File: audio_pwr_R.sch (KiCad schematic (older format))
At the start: 40 parts, among them Q201 BC546, Q202 BC546, Q203 BC546, Q204 BD140, Q205 BC546, Q206 BD139, Q207 BD140, Q208 MJL21193, Q209 MJL21194

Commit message: Opened on home office computer. Some rescue and lib conversion happened. Need to confirm no changes on work laptop.
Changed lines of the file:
@@
 EESchema Schematic File Version 4
-LIBS:AAMB-cache
 EELAYER 30 0
 EELAYER END
@@
 	2600 3650 2450 3650
 $Comp
-L Power-amp:+35V #PWR0110
+L AAMB-rescue:+35V-Power-amp #PWR0110
 U 1 1 5E2254A5
 P 8025 1725
@@
 	8025 1900 8025 1725
 $Comp
-L Power-amp:-35V #PWR0111
+L AAMB-rescue:-35V-Power-amp #PWR0111
 U 1 1 5E229770
 P 8025 5100

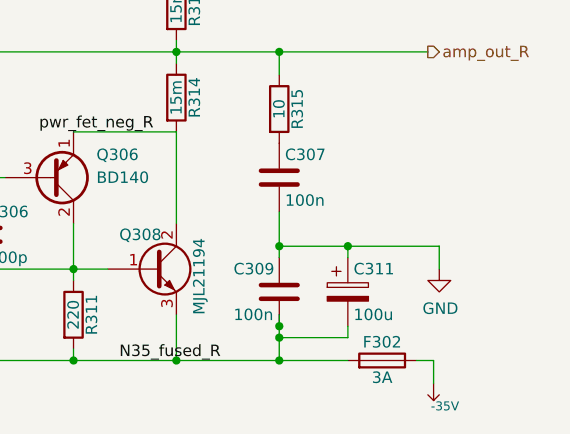
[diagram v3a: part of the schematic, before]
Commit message: Fixed several DRC errors. Tied audoi input returns to GND. Added Switch logic.
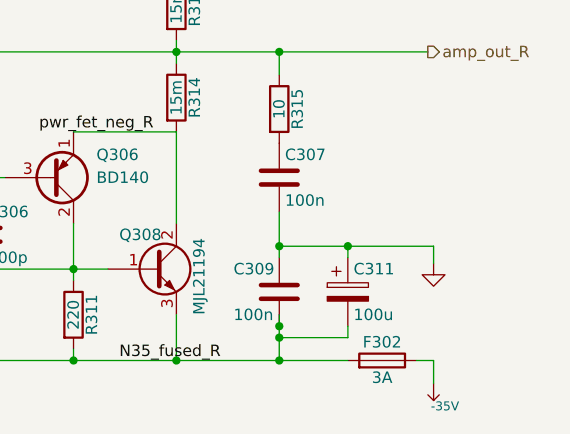
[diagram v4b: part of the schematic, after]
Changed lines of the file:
@@
 EESchema Schematic File Version 4
+LIBS:AAMB-cache
 EELAYER 30 0
 EELAYER END
@@
 Wire Wire Line
 	7300 2050 7300 2100
-Connection ~ 7650 4500
 Connection ~ 3300 3800
 Wire Wire Line
@@
 Wire Wire Line
 	7450 2450 7450 2500
-$Comp
-L power:GND #PWR04
-U 1 1 5C7F686C
-P 8050 4600
-AR Path="/5C7F608F/5C7F686C" Ref="#PWR04"  Part="1"
-AR Path="/5C814038/5C7F686C" Ref="#PWR0304"  Part="1"
-AR Path="/5E252703/5C7F686C" Ref="#PWR?"  Part="1"
-F 0 "#PWR0304" H 8050 4350 50  0001 C CNN
-F 1 "GND" H 8055 4427 50  0000 C CNN
-F 2 "" H 8050 4600 50  0001 C CNN
-F 3 "" H 8050 4600 50  0001 C CNN
-	1    8050 4600
-	1    0    0    -1
-$EndComp
-Wire Wire Line
-	8050 4500 7650 4500
-Wire Wire Line
-	8050 4600 8050 4500
 Wire Wire Line
 	7950 1900 8025 1900
@@
 Wire Wire Line
 	8025 5100 8025 5000
+$Comp
+L power:GND #PWR0120
+U 1 1 5E35DB04
+P 8025 4575
+F 0 "#PWR0120" H 8025 4325 50  0001 C CNN
+F 1 "GND" H 8025 4425 50  0001 C CNN
+F 2 "" H 8025 4575 50  0001 C CNN
+F 3 "" H 8025 4575 50  0001 C CNN
+	1    8025 4575
+	1    0    0    -1
+$EndComp
+Wire Wire Line
+	8025 4575 8025 4500
+Wire Wire Line
+	8025 4500 7650 4500
+Connection ~ 7650 4500
 $EndSCHEMATC

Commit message: 23JAN2020 daily commit.
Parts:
- R214, R215: footprint Resistor_THT:R_Axial_Power_L25.0mm_W9.0mm_P30.48mm -> Resistor_THT:R_Axial_Power_L25.0mm_W9.0mm_P10.16mm_Vertical
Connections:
- net amp_out_R: now also R215.2; no longer R215.1
- net pwr_fet_neg_R: now also R215.1; no longer R215.2
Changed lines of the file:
@@
 F 0 "R314" V 6980 3850 50  0000 C CNN
 F 1 "15m" V 6900 3850 50  0000 C CNN
-F 2 "Resistor_THT:R_Axial_Power_L25.0mm_W9.0mm_P30.48mm" V 6830 3850 50  0001 C CNN
+F 2 "Resistor_THT:R_Axial_Power_L25.0mm_W9.0mm_P10.16mm_Vertical" V 6830 3850 50  0001 C CNN
 F 3 "" H 6900 3850 50  0001 C CNN
 	1    6900 3850
-	1    0    0    -1
+	-1   0    0    1
 $EndComp
 $Comp
@@
 F 0 "R313" V 6980 3450 50  0000 C CNN
 F 1 "15m" V 6900 3450 50  0000 C CNN
-F 2 "Resistor_THT:R_Axial_Power_L25.0mm_W9.0mm_P30.48mm" V 6830 3450 50  0001 C CNN
+F 2 "Resistor_THT:R_Axial_Power_L25.0mm_W9.0mm_P10.16mm_Vertical" V 6830 3450 50  0001 C CNN
 F 3 "" H 6900 3450 50  0001 C CNN
 	1    6900 3450
@@
 	8025 4500 7650 4500
 Connection ~ 7650 4500
+Connection ~ 6900 4000
 $EndSCHEMATC
